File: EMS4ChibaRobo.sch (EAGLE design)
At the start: 25 parts, among them CON1 XT60PB-F, CON2 XT60PB-M, CON3 XT60PB-M, CON4 XT60PB-M, CON5 XT60PB-M, IC1 7805DT, Q1 BUZ11BH, U9 XC6206

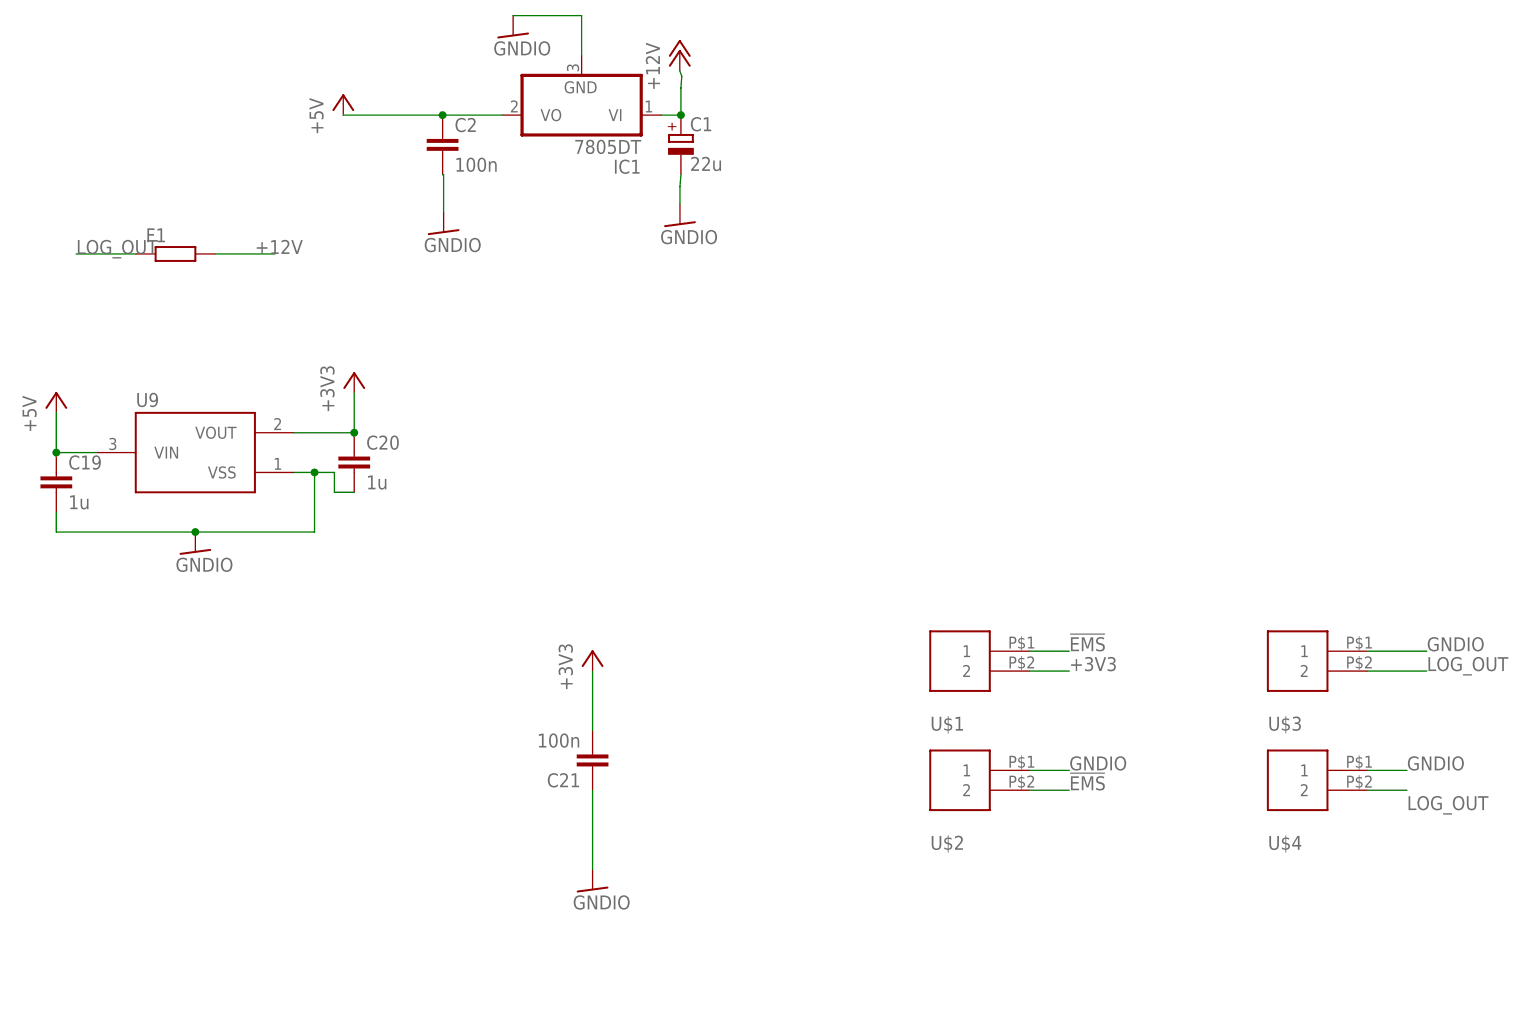
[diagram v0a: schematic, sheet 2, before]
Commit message: 5V駆動に変更
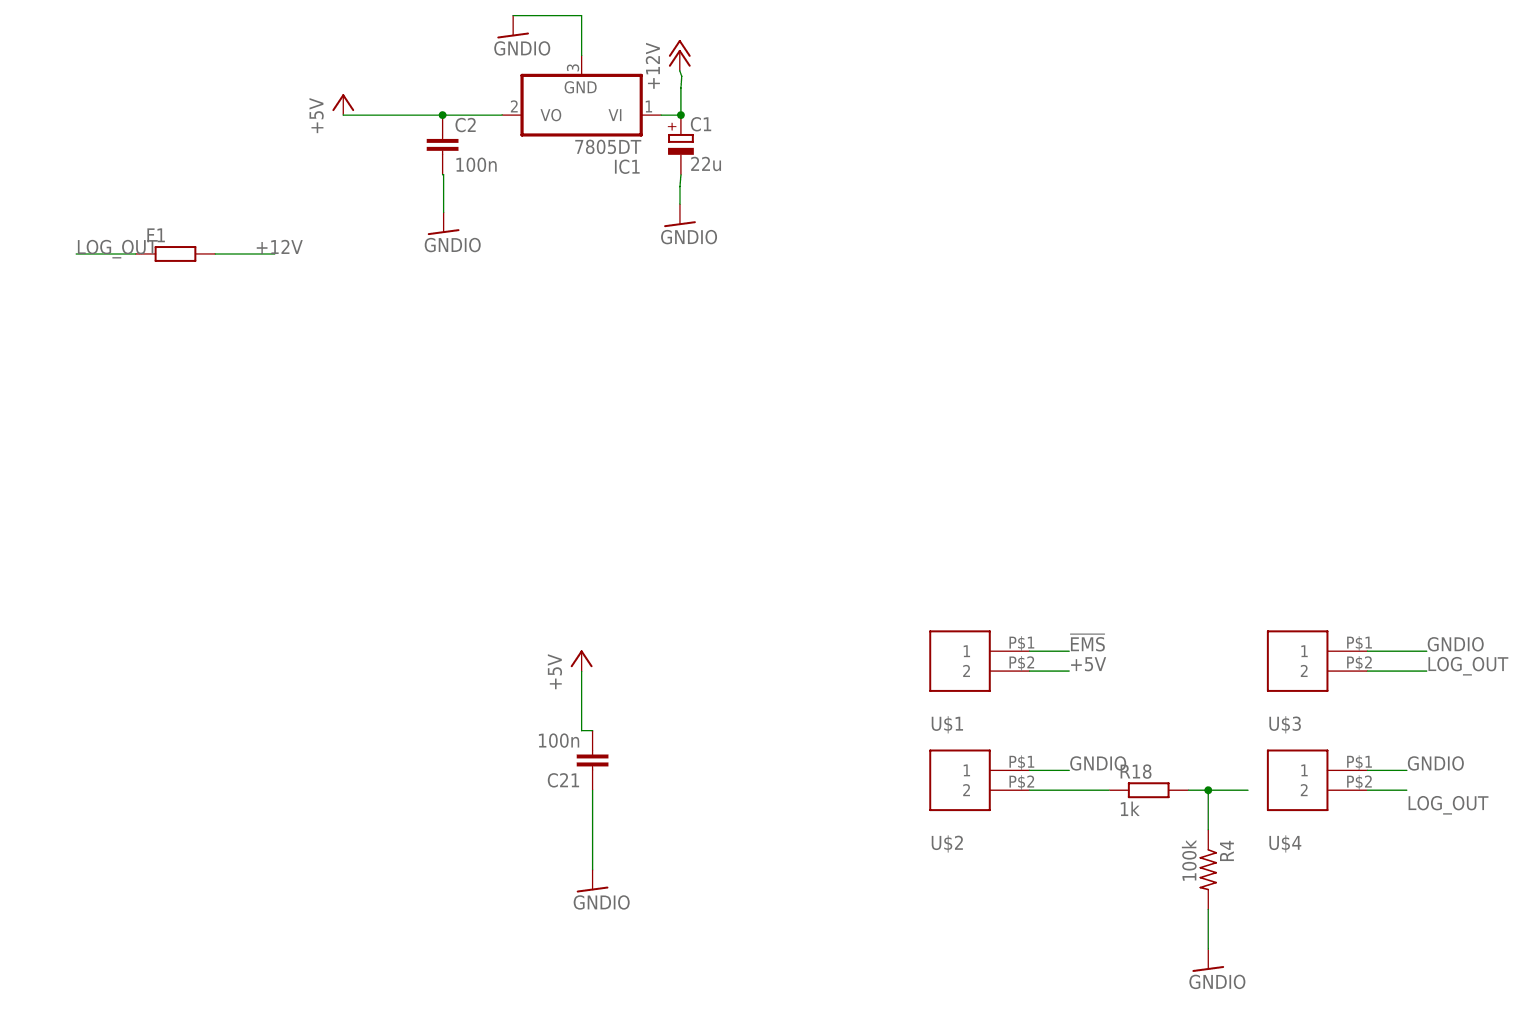
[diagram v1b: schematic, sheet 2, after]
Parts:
- removed C19, C20: 1u, rcl:C-EUC0603
- removed U9: XC6206, torex:XC6206
- added R18: 1k, rcl:R-EU_R0603
- added R4: 100k, rcl:R-US_R0603
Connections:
- removed net +3V3: C20.1, C21.2, U$1.2, U9.VOUT
- new net !EMS1: R18.1, U$2.2
- net !EMS: now also R18.2, R4.1; no longer U$2.2
- net +5V: now also C21.2, U$1.2; no longer C19.1, U9.VIN
- net GNDIO: now also R4.2; no longer C19.2, C20.2, U9.VSS
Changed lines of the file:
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@@
 </variantdefs>
 <classes>
-<class number="0" name="default" width="0.5" drill="0">
+<class number="0" name="default" width="0" drill="0">
 </class>
 <class number="1" name="12v" width="1.5" drill="0">
@@
 <part name="C21" library="rcl" deviceset="C-EU" device="C0603" value="100n"/>
 <part name="F1" library="rcl" library_urn="urn:adsk.eagle:library:334" deviceset="R-EU_" device="R1206" package3d_urn="urn:adsk.eagle:package:23540/2"/>
-<part name="+3V3" library="supply1" library_urn="urn:adsk.eagle:library:371" deviceset="+3V3" device=""/>
 <part name="GND11" library="supply1" library_urn="urn:adsk.eagle:library:371" deviceset="GNDIO" device=""/>
-<part name="U9" library="torex" deviceset="XC6206" device="" package3d_urn="urn:adsk.eagle:package:6993131/1"/>
-<part name="C19" library="rcl" library_urn="urn:adsk.eagle:library:334" deviceset="C-EU" device="C0603" package3d_urn="urn:adsk.eagle:package:23616/2" value="1u"/>
-<part name="C20" library="rcl" library_urn="urn:adsk.eagle:library:334" deviceset="C-EU" device="C0603" package3d_urn="urn:adsk.eagle:package:23616/2" value="1u"/>
-<part name="P+9" library="supply1" library_urn="urn:adsk.eagle:library:371" deviceset="+5V" device=""/>
-<part name="+3V2" library="supply1" library_urn="urn:adsk.eagle:library:371" deviceset="+3V3" device=""/>
 <part name="P+11" library="supply1" library_urn="urn:adsk.eagle:library:371" deviceset="+12V" device=""/>
 <part name="GND4" library="supply1" library_urn="urn:adsk.eagle:library:371" deviceset="GNDIO" device=""/>
 <part name="GND5" library="supply1" library_urn="urn:adsk.eagle:library:371" deviceset="GNDIO" device=""/>
 <part name="GND3" library="supply1" library_urn="urn:adsk.eagle:library:371" deviceset="GNDIO" device=""/>
-<part name="GND8" library="supply1" library_urn="urn:adsk.eagle:library:371" deviceset="GNDIO" device=""/>
 <part name="CON1" library="amass" deviceset="XT60" device="PB-F"/>
 <part name="CON2" library="amass" deviceset="XT60" device="PB-M"/>
@@
 <part name="CON5" library="amass" deviceset="XT60" device="PB-M"/>
 <part name="S1" library="relay" deviceset="897-1AH-C-001" device=""/>
+<part name="P+7" library="supply1" library_urn="urn:adsk.eagle:library:371" deviceset="+5V" device=""/>
+<part name="R18" library="rcl" library_urn="urn:adsk.eagle:library:334" deviceset="R-EU_" device="R0603" package3d_urn="urn:adsk.eagle:package:23555/3" value="1k"/>
+<part name="R4" library="rcl" library_urn="urn:adsk.eagle:library:334" deviceset="R-US_" device="R0603" package3d_urn="urn:adsk.eagle:package:23555/3" value="100k"/>
+<part name="GND2" library="supply1" library_urn="urn:adsk.eagle:library:371" deviceset="GNDIO" device=""/>
 </parts>
 <sheets>
@@
 <attribute name="VALUE" x="-24.13" y="141.478" size="1.778" layer="96"/>
 </instance>
-<instance part="+3V3" gate="G$1" x="33.02" y="93.98" smashed="yes">
-<attribute name="VALUE" x="30.48" y="88.9" size="1.778" layer="96" rot="R90"/>
-</instance>
 <instance part="GND11" gate="G$1" x="33.02" y="63.5" smashed="yes">
 <attribute name="VALUE" x="30.48" y="60.96" size="1.778" layer="96"/>
 </instance>
-<instance part="U9" gate="G$1" x="-17.78" y="119.38" smashed="yes">
-<attribute name="NAME" x="-25.4" y="127" size="1.778" layer="95" rot="MR180"/>
-</instance>
-<instance part="C19" gate="G$1" x="-35.56" y="116.84" smashed="yes">
-<attribute name="NAME" x="-34.036" y="117.221" size="1.778" layer="95"/>
-<attribute name="VALUE" x="-34.036" y="112.141" size="1.778" layer="96"/>
-</instance>
-<instance part="C20" gate="G$1" x="2.54" y="119.38" smashed="yes">
-<attribute name="NAME" x="4.064" y="119.761" size="1.778" layer="95"/>
-<attribute name="VALUE" x="4.064" y="114.681" size="1.778" layer="96"/>
-</instance>
-<instance part="P+9" gate="1" x="-35.56" y="127" smashed="yes">
-<attribute name="VALUE" x="-38.1" y="121.92" size="1.778" layer="96" rot="R90"/>
-</instance>
-<instance part="+3V2" gate="G$1" x="2.54" y="129.54" smashed="yes">
-<attribute name="VALUE" x="0" y="124.46" size="1.778" layer="96" rot="R90"/>
-</instance>
 <instance part="P+11" gate="1" x="44.172" y="170.75" smashed="yes">
 <attribute name="VALUE" x="41.632" y="165.67" size="1.778" layer="96" rot="R90"/>
@@
 <instance part="GND3" gate="G$1" x="22.86" y="172.72" smashed="yes">
 <attribute name="VALUE" x="20.32" y="170.18" size="1.778" layer="96"/>
-</instance>
-<instance part="GND8" gate="G$1" x="-17.78" y="106.68" smashed="yes">
-<attribute name="VALUE" x="-20.32" y="104.14" size="1.778" layer="96"/>
 </instance>
 <instance part="U$1" gate="G$1" x="81.28" y="93.98" smashed="yes">
@@
 <attribute name="NAME" x="15.364" y="160.381" size="1.778" layer="95"/>
 <attribute name="VALUE" x="15.364" y="155.301" size="1.778" layer="96"/>
+</instance>
+<instance part="P+7" gate="1" x="31.62" y="93.96" smashed="yes">
+<attribute name="VALUE" x="29.08" y="88.88" size="1.778" layer="96" rot="R90"/>
+</instance>
+<instance part="R18" gate="G$1" x="104.14" y="76.2" smashed="yes">
+<attribute name="NAME" x="100.33" y="77.6986" size="1.778" layer="95"/>
+<attribute name="VALUE" x="100.33" y="72.898" size="1.778" layer="96"/>
+</instance>
+<instance part="R4" gate="G$1" x="111.76" y="66.04" smashed="yes" rot="R270">
+<attribute name="NAME" x="113.2586" y="69.85" size="1.778" layer="95" rot="R270"/>
+<attribute name="VALUE" x="108.458" y="69.85" size="1.778" layer="96" rot="R270"/>
+</instance>
+<instance part="GND2" gate="G$1" x="111.76" y="53.34" smashed="yes">
+<attribute name="VALUE" x="109.22" y="50.8" size="1.778" layer="96"/>
 </instance>
 </instances>
@@
 </segment>
 <segment>
-<pinref part="C19" gate="G$1" pin="2"/>
-<wire x1="-35.56" y1="111.76" x2="-35.56" y2="109.22" width="0.1524" layer="91"/>
-<wire x1="-35.56" y1="109.22" x2="-17.78" y2="109.22" width="0.1524" layer="91"/>
-<pinref part="U9" gate="G$1" pin="VSS"/>
-<wire x1="-17.78" y1="109.22" x2="-2.54" y2="109.22" width="0.1524" layer="91"/>
-<wire x1="-5.08" y1="116.84" x2="-2.54" y2="116.84" width="0.1524" layer="91"/>
-<pinref part="C20" gate="G$1" pin="2"/>
-<wire x1="-2.54" y1="116.84" x2="0" y2="116.84" width="0.1524" layer="91"/>
-<wire x1="0" y1="116.84" x2="0" y2="114.3" width="0.1524" layer="91"/>
-<wire x1="0" y1="114.3" x2="2.54" y2="114.3" width="0.1524" layer="91"/>
-<wire x1="-2.54" y1="109.22" x2="-2.54" y2="116.84" width="0.1524" layer="91"/>
-<junction x="-2.54" y="116.84"/>
-<pinref part="GND8" gate="G$1" pin="GNDIO"/>
-<junction x="-17.78" y="109.22"/>
-</segment>
-<segment>
 <pinref part="U$4" gate="G$1" pin="1"/>
 <wire x1="137.16" y1="78.74" x2="132.08" y2="78.74" width="0.1524" layer="91"/>
@@
 <wire x1="31.62" y1="175.26" x2="22.86" y2="175.26" width="0.1524" layer="91"/>
 </segment>
-</net>
-<net name="+3V3" class="0">
-<segment>
-<pinref part="C21" gate="G$1" pin="2"/>
-<wire x1="33.02" y1="91.44" x2="33.02" y2="83.82" width="0.1524" layer="91"/>
-<pinref part="+3V3" gate="G$1" pin="+3V3"/>
-</segment>
-<segment>
-<pinref part="U9" gate="G$1" pin="VOUT"/>
-<wire x1="-5.08" y1="121.92" x2="2.54" y2="121.92" width="0.1524" layer="91"/>
-<pinref part="+3V2" gate="G$1" pin="+3V3"/>
-<wire x1="2.54" y1="121.92" x2="2.54" y2="127" width="0.1524" layer="91"/>
-<pinref part="C20" gate="G$1" pin="1"/>
-<junction x="2.54" y="121.92"/>
-</segment>
-<segment>
-<pinref part="U$1" gate="G$1" pin="2"/>
-<wire x1="88.9" y1="91.44" x2="93.98" y2="91.44" width="0.1524" layer="91"/>
-<label x="93.98" y="91.44" size="1.778" layer="95"/>
+<segment>
+<pinref part="R4" gate="G$1" pin="2"/>
+<wire x1="111.76" y1="60.96" x2="111.76" y2="55.88" width="0.1524" layer="91"/>
+<pinref part="GND2" gate="G$1" pin="GNDIO"/>
 </segment>
 </net>
@@
 </segment>
 <segment>
-<pinref part="U$2" gate="G$1" pin="2"/>
-<wire x1="88.9" y1="76.2" x2="93.98" y2="76.2" width="0.1524" layer="91"/>
-<label x="93.98" y="76.2" size="1.778" layer="95"/>
+<pinref part="R18" gate="G$1" pin="2"/>
+<wire x1="109.22" y1="76.2" x2="111.76" y2="76.2" width="0.1524" layer="91"/>
+<pinref part="R4" gate="G$1" pin="1"/>
+<wire x1="111.76" y1="76.2" x2="116.84" y2="76.2" width="0.1524" layer="91"/>
+<wire x1="111.76" y1="71.12" x2="111.76" y2="76.2" width="0.1524" layer="91"/>
+<junction x="111.76" y="76.2"/>
 </segment>
 </net>
@@
 <net name="+5V" class="0">
 <segment>
-<pinref part="P+9" gate="1" pin="+5V"/>
-<wire x1="-35.56" y1="124.46" x2="-35.56" y2="119.38" width="0.1524" layer="91"/>
-<pinref part="U9" gate="G$1" pin="VIN"/>
-<wire x1="-35.56" y1="119.38" x2="-30.48" y2="119.38" width="0.1524" layer="91"/>
-<pinref part="C19" gate="G$1" pin="1"/>
-<junction x="-35.56" y="119.38"/>
-</segment>
-<segment>
 <pinref part="P+3" gate="1" pin="+5V"/>
 <wire x1="1.14" y1="162.54" x2="13.84" y2="162.54" width="0.1524" layer="91"/>
@@
 <junction x="13.84" y="162.54"/>
 </segment>
+<segment>
+<pinref part="C21" gate="G$1" pin="2"/>
+<pinref part="P+7" gate="1" pin="+5V"/>
+<wire x1="33.02" y1="83.82" x2="31.62" y2="83.82" width="0.1524" layer="91"/>
+<wire x1="31.62" y1="83.82" x2="31.62" y2="91.42" width="0.1524" layer="91"/>
+</segment>
+<segment>
+<pinref part="U$1" gate="G$1" pin="2"/>
+<wire x1="88.9" y1="91.44" x2="93.98" y2="91.44" width="0.1524" layer="91"/>
+<label x="93.98" y="91.44" size="1.778" layer="95"/>
+</segment>
 </net>
 <net name="LOG_OUT" class="2">
@@
 </segment>
 </net>
+<net name="!EMS1" class="0">
+<segment>
+<pinref part="R18" gate="G$1" pin="1"/>
+<wire x1="99.06" y1="76.2" x2="88.9" y2="76.2" width="0.1524" layer="91"/>
+<pinref part="U$2" gate="G$1" pin="2"/>
+</segment>
+</net>

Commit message: update
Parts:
- removed S1: 897-1AH-C-001, relay:897-1AH-C-001
- added U$5: 897-1AH-C-001, CRS_EAGLE_Lib:897-1AH-C-001
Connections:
- net +12V: now also U$5G$1.1; no longer S1U1.1
- net BATT_POWER: now also U$5G$2.O; no longer S1U2.S
- net N$1: now also U$5G$1.2; no longer S1U1.2
- net OUT_POWER_A: now also U$5G$2.P; no longer S1U2.P
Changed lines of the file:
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@@
 <part name="CON4" library="amass" deviceset="XT60" device="PB-M"/>
 <part name="CON5" library="amass" deviceset="XT60" device="PB-M"/>
-<part name="S1" library="relay" deviceset="897-1AH-C-001" device=""/>
 <part name="P+7" library="supply1" library_urn="urn:adsk.eagle:library:371" deviceset="+5V" device=""/>
 <part name="R18" library="rcl" library_urn="urn:adsk.eagle:library:334" deviceset="R-EU_" device="R0603" package3d_urn="urn:adsk.eagle:package:23555/3" value="1k"/>
 <part name="R4" library="rcl" library_urn="urn:adsk.eagle:library:334" deviceset="R-US_" device="R0603" package3d_urn="urn:adsk.eagle:package:23555/3" value="100k"/>
 <part name="GND2" library="supply1" library_urn="urn:adsk.eagle:library:371" deviceset="GNDIO" device=""/>
+<part name="U$5" library="CRS_EAGLE_Lib" deviceset="897-1AH-C-001" device=""/>
 </parts>
 <sheets>
@@
 <attribute name="NAME" x="163.83" y="5.588" size="1.778" layer="95" rot="R180"/>
 </instance>
-<instance part="S1" gate="U1" x="73.66" y="83.82" smashed="yes">
+<instance part="U$5" gate="G$1" x="73.66" y="83.82" smashed="yes">
 <attribute name="VALUE" x="74.93" y="86.741" size="1.778" layer="96"/>
 <attribute name="PART" x="74.93" y="88.9" size="1.778" layer="95"/>
 </instance>
-<instance part="S1" gate="U2" x="104.14" y="68.58" smashed="yes">
+<instance part="U$5" gate="G$2" x="104.14" y="68.58" smashed="yes">
 <attribute name="PART" x="101.6" y="66.04" size="1.778" layer="95" rot="R90"/>
 </instance>
@@
 <label x="104.14" y="93.98" size="1.778" layer="95"/>
 <wire x1="104.14" y1="73.66" x2="104.14" y2="91.44" width="0.1524" layer="91"/>
-<pinref part="S1" gate="U2" pin="S"/>
+<pinref part="U$5" gate="G$2" pin="O"/>
 </segment>
 <segment>
@@
 <net name="OUT_POWER_A" class="0">
 <segment>
-<label x="104.14" y="60.96" size="1.778" layer="95" rot="R180"/>
-<wire x1="104.14" y1="63.5" x2="104.14" y2="60.96" width="0.1524" layer="91"/>
-<pinref part="S1" gate="U2" pin="P"/>
+<label x="101.6" y="58.42" size="1.778" layer="95" rot="R180"/>
+<pinref part="U$5" gate="G$2" pin="P"/>
+<wire x1="104.14" y1="63.5" x2="104.14" y2="55.88" width="0.1524" layer="91"/>
 </segment>
 <segment>
@@
 <segment>
 <pinref part="P+2" gate="1" pin="+12V"/>
+<pinref part="U$5" gate="G$1" pin="1"/>
 <wire x1="73.66" y1="104.14" x2="73.66" y2="88.9" width="0.1524" layer="91"/>
-<pinref part="S1" gate="U1" pin="1"/>
 </segment>
 </net>
 <net name="N$1" class="0">
 <segment>
+<pinref part="U$5" gate="G$1" pin="2"/>
 <pinref part="Q1" gate="1" pin="D"/>
 <wire x1="73.66" y1="78.74" x2="73.66" y2="73.66" width="0.1524" layer="91"/>
-<pinref part="S1" gate="U1" pin="2"/>
-</segment>
-</net>
+</segment>
+</net>
